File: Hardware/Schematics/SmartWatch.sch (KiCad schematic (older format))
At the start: 104 parts, among them J1 USB_C_Receptacle, J2 PIC32_ICSP, M1 Motor_DC, Q1 Photo_NPN, Q2 2N7000, SW1 SW_Push, SW2 SW_Push, U1 BQ25010, U2 PIC32MZ2048EFG064, U3 STMPE811, U4 nRF8001, U5 LSM303AGR, Y1 80MHz, Y2 32.768kHz, Y3 16MHz

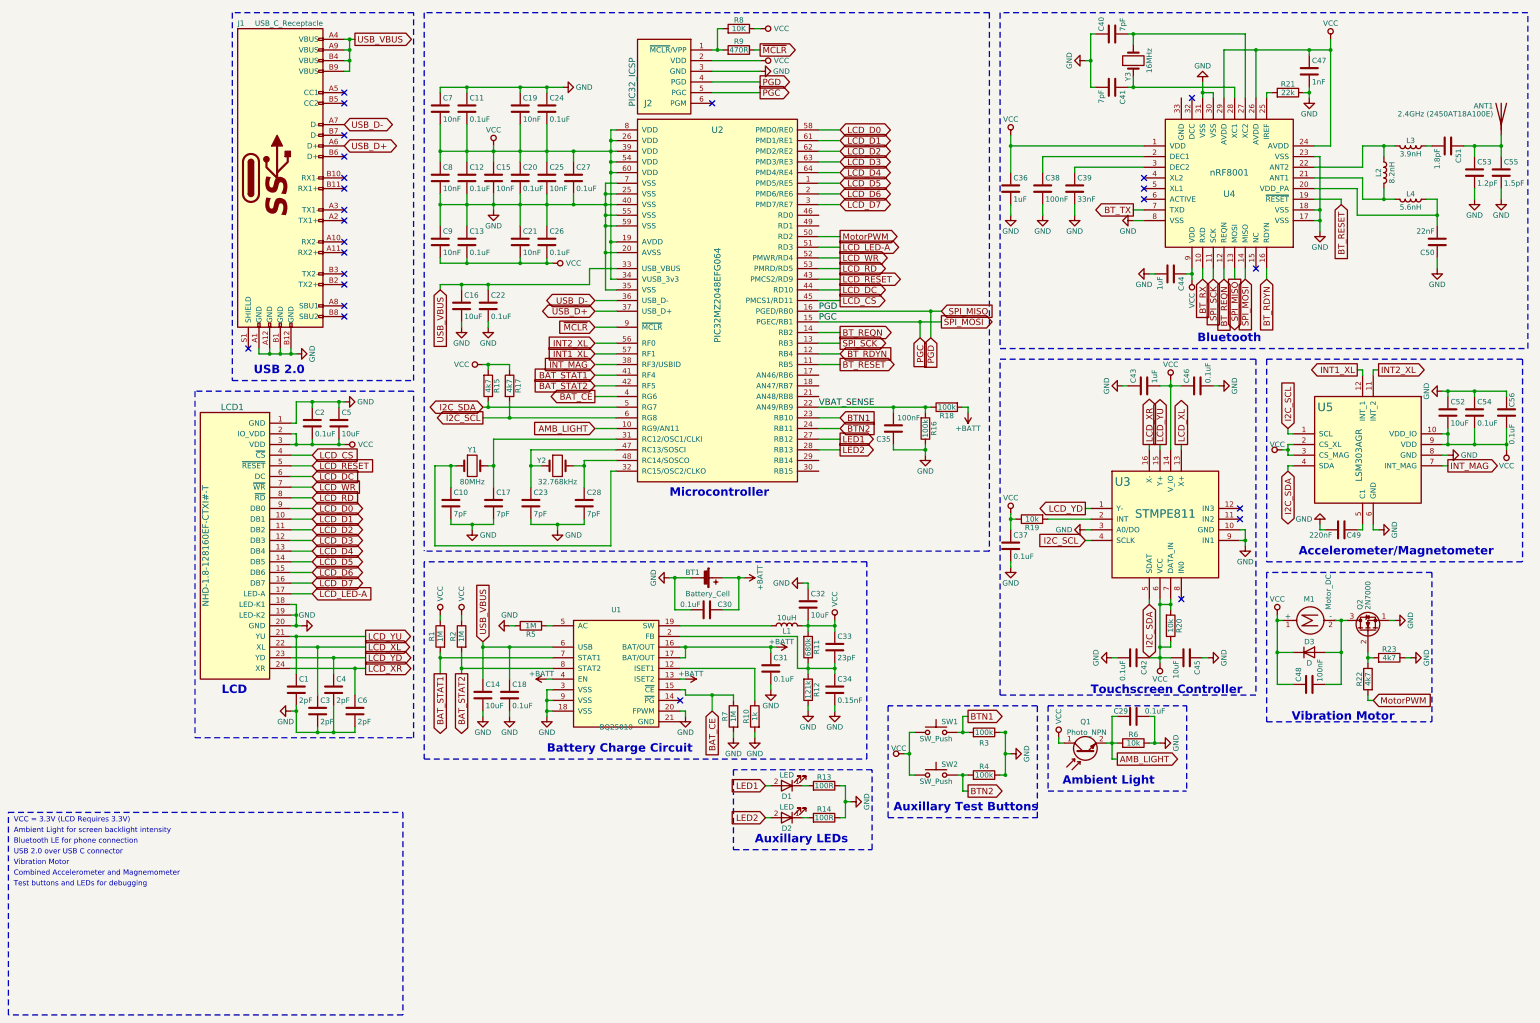
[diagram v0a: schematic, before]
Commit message: fixed file organization
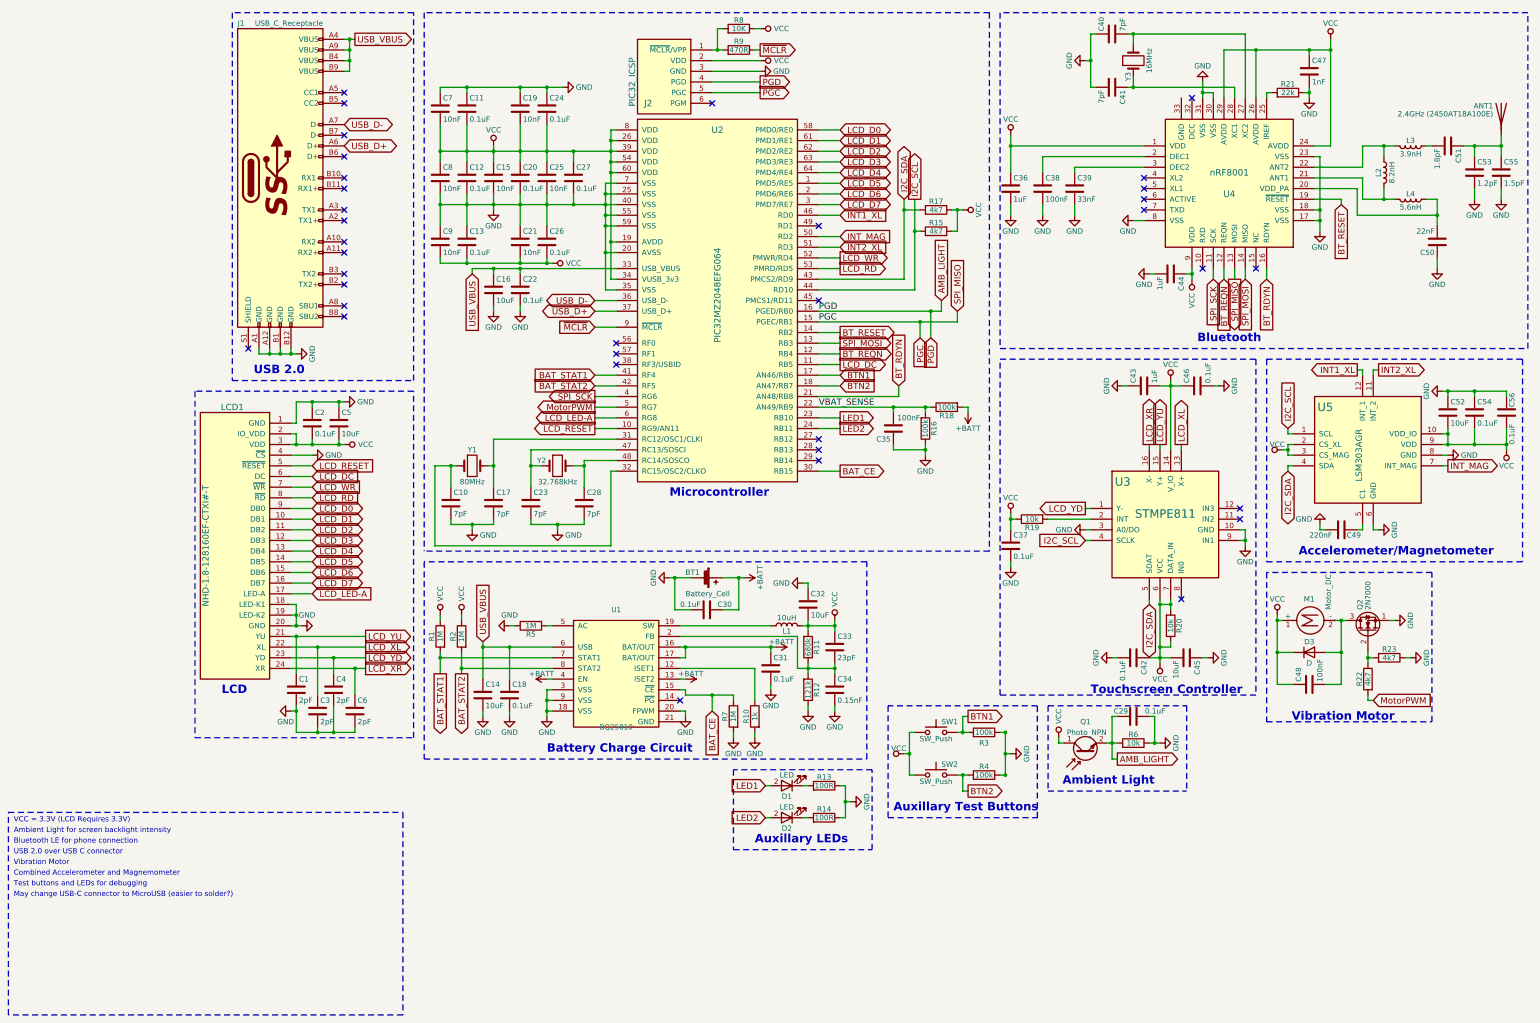
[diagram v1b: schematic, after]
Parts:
- BT1, M1: footprint (none) -> Pin_Headers:Pin_Header_Straight_2x01_Pitch2.54mm_SMD
- C1, C10, C11, C12, C13, C14, C15, C16, C17, C18, C19, C2, C20, C21, C22, C23, C24, C25, C26, C27, C28, C29, C3, C30, C31, C32, C33, C34, C35, C36, C37, C38, C39, C4, C40, C41, C42, C43, C44, C45, C46, C47, C48, C49, C5, C50, C51, C52, C53, C54, C55, C56, C6, C7, C8, C9: footprint (none) -> Capacitors_SMD:C_0805_HandSoldering
- D1, D2: footprint (none) -> LEDs:LED_0805_HandSoldering
- D3: footprint (none) -> Diodes_SMD:D_0805
- J1: footprint (none) -> Connectors_USB:USB_C_Receptacle_Amphenol_12401548E4-2A_CircularHoles
- J2: footprint (none) -> Pin_Headers:Pin_Header_Straight_2x03_Pitch1.00mm_SMD
- L1, L2, L3, L4: footprint (none) -> Inductors_SMD:L_0805_HandSoldering
- Q1: footprint (none) -> Diodes_SMD:D_3220
- R1, R10, R11, R12, R13, R14, R15, R16, R17, R18, R19, R2, R20, R21, R22, R23, R3, R4, R5, R6, R7, R8, R9: footprint (none) -> Resistors_SMD:R_0805_HandSoldering
- SW1, SW2: footprint (none) -> Buttons_Switches_SMD:SW_SPST_FSMSM
- U1: footprint (none) -> Schematics:pvqfn-n20
- U2: footprint (none) -> Housings_QFP:TQFP-64_10x10mm_Pitch0.5mm
- U3: footprint (none) -> Housings_DFN_QFN:QFN-20-1EP_4x4mm_Pitch0.5mm
- U4: footprint (none) -> Housings_DFN_QFN:QFN-32-1EP_5x5mm_Pitch0.5mm
- U5: footprint (none) -> Housings_LGA:LGA-12_2x2mm_Pitch0.5mm
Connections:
- net AMB_LIGHT: now also J2.4 (PGD), U2.16 (PGED/RB0); no longer U2.10 (RG9/AN11)
- net BAT_CE: now also U2.30 (RB15); no longer U2.4 (RG6)
- net BTN1: now also U2.17 (AN46/RB6); no longer U2.23 (RB10)
- net BTN2: now also U2.18 (AN47/RB7); no longer U2.24 (RB11)
- net BT_RDYN: now also U2.21 (AN48/RB8); no longer U2.12 (RB4)
- net BT_REQN: now also U2.12 (RB4); no longer U2.14 (RB2)
- net BT_RESET: now also U2.14 (RB2); no longer U2.11 (RB5)
- net GND: now also LCD1.4 (~CS)
- net I2C_SCL: now also R15.2, U2.44 (RD10); no longer R17.2, U2.6 (RG8)
- net I2C_SDA: now also R17.2, U2.43 (PMCS2/RD9); no longer R15.1, U2.5 (RG7)
- net INT1_XL: now also U2.46 (RD0); no longer U2.57 (RF1)
- net INT2_XL: now also U2.51 (RD3); no longer U2.56 (RF0)
- net INT_MAG: now also U2.50 (RD2); no longer U2.38 (RF3/USBID)
- net LCD_DC: now also U2.11 (RB5); no longer U2.44 (RD10)
- net LCD_LED-A: now also U2.6 (RG8); no longer U2.51 (RD3)
- net LCD_RESET: now also U2.10 (RG9/AN11); no longer U2.43 (PMCS2/RD9)
- net LED1: now also U2.23 (RB10); no longer U2.27 (RB12)
- net LED2: now also U2.24 (RB11); no longer U2.28 (RB13)
- net MotorPWM: now also U2.5 (RG7); no longer U2.50 (RD2)
- net PGC: now also U4.13 (MOSI); no longer U4.14 (MISO)
- net SPI_SCK: now also U2.4 (RG6); no longer U2.13 (RB3)
- net VCC: now also R15.1; no longer R15.2
- net BT_RX: no longer names the net of U4.10 (RXD)
- net BT_TX: no longer names the net of U4.7 (TXD)
- net LCD_CS: no longer names the net of U2.45 (PMCS1/RD11)
- net LCD_CS: no longer LCD1.4 (~CS)
- removed net PGD: J2.4 (PGD), U2.16 (PGED/RB0), U4.13 (MOSI)
- new net SPI_MOSI: U2.13 (RB3), U4.14 (MISO)
- no-connect marks 25 -> 35
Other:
- note added: "May change USB-C connector to MicroUSB (easier to solder?)"
- moved on the sheet: C16, C22, R15, R17

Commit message: finish footprint selecting and started pcb
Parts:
- removed Y3: 16MHz, symbol Crystal
- added Y3: Crystal_GND24, symbol Crystal_GND24
- ANT1: footprint (none) -> 2450AT18A100E:2450AT18A100E
- C10, C17: value 7pF -> 20pF
- C23, C28: value 7pF -> 12.5pF
- C40, C41: value 7pF -> 10pF
- Y1: value 80MHz -> 64MHz; footprint (none) -> Crystals:Crystal_SMD_HC49-SD_HandSoldering
- Y2: footprint (none) -> 2450AT18A100E:TFA322PG327KR
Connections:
- net GND: now also Y3.2, Y3.4
- net at C40.2, U4.27 (XC2): now also Y3.1
- net at C41.1, U4.28 (XC1): now also Y3.3

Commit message: Working on schematic
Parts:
- removed C11, C12, C13, C22, C31: 0.1uF, Capacitors_SMD:C_0805_HandSoldering, symbol C
- removed C16: 10uF, Capacitors_SMD:C_0805_HandSoldering, symbol C
- removed C35: 100nF, Capacitors_SMD:C_0805_HandSoldering, symbol C
- removed C7, C8, C9: 10nF, Capacitors_SMD:C_0805_HandSoldering, symbol C
- removed R20: 10k, Resistors_SMD:R_0805_HandSoldering, symbol R
- C1: renamed from C40; footprint Capacitors_SMD:C_0805_HandSoldering -> Capacitors_SMD:C_0603
- C10: renamed from C20; footprint Capacitors_SMD:C_0805_HandSoldering -> Capacitors_SMD:C_0603
- C11: renamed from C25; footprint Capacitors_SMD:C_0805_HandSoldering -> Capacitors_SMD:C_0603
- C12: renamed from C27; footprint Capacitors_SMD:C_0805_HandSoldering -> Capacitors_SMD:C_0603
- C13: renamed from C36; footprint Capacitors_SMD:C_0805_HandSoldering -> Capacitors_SMD:C_0603
- C14: renamed from C38; footprint Capacitors_SMD:C_0805_HandSoldering -> Capacitors_SMD:C_0603
- C15: renamed from C39; footprint Capacitors_SMD:C_0805_HandSoldering -> Capacitors_SMD:C_0603
- C16: renamed from C21; footprint Capacitors_SMD:C_0805_HandSoldering -> Capacitors_SMD:C_0603
- C17: renamed from C26; footprint Capacitors_SMD:C_0805_HandSoldering -> Capacitors_SMD:C_0603
- C18: renamed from C50; footprint Capacitors_SMD:C_0805_HandSoldering -> Capacitors_SMD:C_0603
- C19: renamed from C44; footprint Capacitors_SMD:C_0805_HandSoldering -> Capacitors_SMD:C_0603
- C2: renamed from C47; footprint Capacitors_SMD:C_0805_HandSoldering -> Capacitors_SMD:C_0603
- C20: renamed from C43; footprint Capacitors_SMD:C_0805_HandSoldering -> Capacitors_SMD:C_0603
- C21: renamed from C46; footprint Capacitors_SMD:C_0805_HandSoldering -> Capacitors_SMD:C_0603
- C22: renamed from C52; footprint Capacitors_SMD:C_0805_HandSoldering -> Capacitors_SMD:C_0603
- C23: renamed from C54; footprint Capacitors_SMD:C_0805_HandSoldering -> Capacitors_SMD:C_0603
- C24: renamed from C56; footprint Capacitors_SMD:C_0805_HandSoldering -> Capacitors_SMD:C_0603
- C25: renamed from C2; footprint Capacitors_SMD:C_0805_HandSoldering -> Capacitors_SMD:C_0603
- C26: renamed from C5; footprint Capacitors_SMD:C_0805_HandSoldering -> Capacitors_SMD:C_0603
- C28: renamed from C10; footprint Capacitors_SMD:C_0805_HandSoldering -> Capacitors_SMD:C_0603
- C29: renamed from C17; footprint Capacitors_SMD:C_0805_HandSoldering -> Capacitors_SMD:C_0603
- C3: renamed from C41; footprint Capacitors_SMD:C_0805_HandSoldering -> Capacitors_SMD:C_0603
- C30: renamed from C23; footprint Capacitors_SMD:C_0805_HandSoldering -> Capacitors_SMD:C_0603
- C31: renamed from C28; footprint Capacitors_SMD:C_0805_HandSoldering -> Capacitors_SMD:C_0603
- C32: renamed from C49; footprint Capacitors_SMD:C_0805_HandSoldering -> Capacitors_SMD:C_0603
- C33: renamed from C37; footprint Capacitors_SMD:C_0805_HandSoldering -> Capacitors_SMD:C_0603
- C34: renamed from C32; footprint Capacitors_SMD:C_0805_HandSoldering -> Capacitors_SMD:C_0603
- C35: renamed from C30; footprint Capacitors_SMD:C_0805_HandSoldering -> Capacitors_SMD:C_0603
- C36: renamed from C33; footprint Capacitors_SMD:C_0805_HandSoldering -> Capacitors_SMD:C_0603
- C37: renamed from C42; footprint Capacitors_SMD:C_0805_HandSoldering -> Capacitors_SMD:C_0603
- C38: renamed from C45; footprint Capacitors_SMD:C_0805_HandSoldering -> Capacitors_SMD:C_0603
- C39: renamed from C48; footprint Capacitors_SMD:C_0805_HandSoldering -> Capacitors_SMD:C_0603
- C4: renamed from C19; footprint Capacitors_SMD:C_0805_HandSoldering -> Capacitors_SMD:C_0603
- C40: renamed from C1; footprint Capacitors_SMD:C_0805_HandSoldering -> Capacitors_SMD:C_0603
- C41: renamed from C4; footprint Capacitors_SMD:C_0805_HandSoldering -> Capacitors_SMD:C_0603
- C42: renamed from C34; footprint Capacitors_SMD:C_0805_HandSoldering -> Capacitors_SMD:C_0603
- C43: renamed from C14; footprint Capacitors_SMD:C_0805_HandSoldering -> Capacitors_SMD:C_0603
- C44: renamed from C18; footprint Capacitors_SMD:C_0805_HandSoldering -> Capacitors_SMD:C_0603
- C45: renamed from C3; footprint Capacitors_SMD:C_0805_HandSoldering -> Capacitors_SMD:C_0603
- C46: renamed from C6; footprint Capacitors_SMD:C_0805_HandSoldering -> Capacitors_SMD:C_0603
- C47: renamed from C29; footprint Capacitors_SMD:C_0805_HandSoldering -> Capacitors_SMD:C_0603
- C5: renamed from C24; footprint Capacitors_SMD:C_0805_HandSoldering -> Capacitors_SMD:C_0603
- C6: renamed from C51; footprint Capacitors_SMD:C_0805_HandSoldering -> Capacitors_SMD:C_0603
- C7: renamed from C53; footprint Capacitors_SMD:C_0805_HandSoldering -> Capacitors_SMD:C_0603
- C8: renamed from C55; footprint Capacitors_SMD:C_0805_HandSoldering -> Capacitors_SMD:C_0603
- C9: renamed from C15; footprint Capacitors_SMD:C_0805_HandSoldering -> Capacitors_SMD:C_0603
- D1: renamed from D3; footprint Diodes_SMD:D_0805 -> Diodes_SMD:D_0603
- D2: renamed from D1; footprint LEDs:LED_0805_HandSoldering -> LEDs:LED_0603
- D3: renamed from D2; footprint LEDs:LED_0805_HandSoldering -> LEDs:LED_0603
- L1: renamed from L3; footprint Inductors_SMD:L_0805_HandSoldering -> Inductors_SMD:L_0603
- L2: footprint Inductors_SMD:L_0805_HandSoldering -> Inductors_SMD:L_0603
- L3: renamed from L4; footprint Inductors_SMD:L_0805_HandSoldering -> Inductors_SMD:L_0603
- L4: renamed from L1; footprint Inductors_SMD:L_0805_HandSoldering -> Inductors_SMD:L_0603
- LCD1: footprint (none) -> 2450AT18A100E:NHD-1.8-128160EF-CTXI#-T
- R1: renamed from R8; footprint Resistors_SMD:R_0805_HandSoldering -> Resistors_SMD:R_0603
- R10: renamed from R1; footprint Resistors_SMD:R_0805_HandSoldering -> Resistors_SMD:R_0603
- R11: renamed from R2; footprint Resistors_SMD:R_0805_HandSoldering -> Resistors_SMD:R_0603
- R12: renamed from R11; footprint Resistors_SMD:R_0805_HandSoldering -> Resistors_SMD:R_0603
- R13: renamed from R23; footprint Resistors_SMD:R_0805_HandSoldering -> Resistors_SMD:R_0603
- R14: renamed from R22; footprint Resistors_SMD:R_0805_HandSoldering -> Resistors_SMD:R_0603
- R15: renamed from R12; footprint Resistors_SMD:R_0805_HandSoldering -> Resistors_SMD:R_0603
- R16: renamed from R7; footprint Resistors_SMD:R_0805_HandSoldering -> Resistors_SMD:R_0603
- R17: renamed from R10; footprint Resistors_SMD:R_0805_HandSoldering -> Resistors_SMD:R_0603
- R18: renamed from R3; footprint Resistors_SMD:R_0805_HandSoldering -> Resistors_SMD:R_0603
- R19: renamed from R6; footprint Resistors_SMD:R_0805_HandSoldering -> Resistors_SMD:R_0603
- R2: renamed from R9; footprint Resistors_SMD:R_0805_HandSoldering -> Resistors_SMD:R_0603
- R20: renamed from R4; footprint Resistors_SMD:R_0805_HandSoldering -> Resistors_SMD:R_0603
- R21: renamed from R13; footprint Resistors_SMD:R_0805_HandSoldering -> Resistors_SMD:R_0603
- R22: renamed from R14; footprint Resistors_SMD:R_0805_HandSoldering -> Resistors_SMD:R_0603
- R3: renamed from R21; footprint Resistors_SMD:R_0805_HandSoldering -> Resistors_SMD:R_0603
- R4: renamed from R17; footprint Resistors_SMD:R_0805_HandSoldering -> Resistors_SMD:R_0603
- R5: renamed from R15; footprint Resistors_SMD:R_0805_HandSoldering -> Resistors_SMD:R_0603
- R6: renamed from R18; footprint Resistors_SMD:R_0805_HandSoldering -> Resistors_SMD:R_0603
- R7: renamed from R16; footprint Resistors_SMD:R_0805_HandSoldering -> Resistors_SMD:R_0603
- R8: renamed from R19; footprint Resistors_SMD:R_0805_HandSoldering -> Resistors_SMD:R_0603
- R9: renamed from R5; footprint Resistors_SMD:R_0805_HandSoldering -> Resistors_SMD:R_0603
- Y1: renamed from Y3; footprint (none) -> 2450AT18A100E:CX2520DB16000F0FDFC1
- Y2: renamed from Y1; footprint Crystals:Crystal_SMD_HC49-SD_HandSoldering -> 2450AT18A100E:CX2520DB16000F0FDFC1
- renumbered J2 to J1, J1 to J2, Q2 to Q1, Q1 to Q2, U4 to U1, U5 to U3, U3 to U4, U1 to U5, Y2 to Y3

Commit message: PCB
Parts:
- removed Y2: 64MHz, 2450AT18A100E:CX2520DB16000F0FDFC1, symbol Crystal
- added Y?: Crystal_GND24, 2450AT18A100E:CX2520DB16000F0FDFC1, symbol Crystal_GND24
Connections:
- net GND: now also Y?.2, Y?.4
- net at C29.1, U2.31 (RC12/OSC1/CLKI): now also Y?.1
- net at C28.1, U2.32 (RC15/OSC2/CLKO): now also Y?.3
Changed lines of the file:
@@
 $EndComp
 $Comp
-L Crystal Y2
-U 1 1 5A2813FF
-P 4900 6000
-F 0 "Y2" H 4900 6150 50  0000 C CNN
-F 1 "64MHz" H 4900 5850 50  0000 C CNN
-F 2 "2450AT18A100E:CX2520DB16000F0FDFC1" H 4900 6000 50  0001 C CNN
-F 3 "" H 4900 6000 50  0001 C CNN
-	1    4900 6000
-	1    0    0    -1
-$EndComp
-$Comp
 L C C28
 U 1 1 5A281E18
@@
 	4700 6550 4700 6500
 Wire Wire Line
-	4900 6550 4900 6600
+	4900 6200 4900 6600
 Wire Wire Line
 	4700 6550 5100 6550
@@
 	12050 2450 12050 2550
 Wire Wire Line
-	11050 2450 12050 2450
-Connection ~ 11100 2450
-Wire Wire Line
-	11100 2350 11100 2450
-Wire Wire Line
-	11100 2050 11100 1950
-Wire Wire Line
-	11050 1950 12150 1950
-Wire Wire Line
 	12150 1950 12150 2550
-Connection ~ 11100 1950
 Wire Wire Line
 	10700 1950 10700 2450
@@
 Wire Wire Line
 	11450 7300 11450 7250
+Wire Wire Line
+	12050 2450 11050 2450
+Wire Wire Line
+	11050 1950 12150 1950
+Wire Wire Line
+	11100 2050 11100 1950
+Connection ~ 11100 1950
+Wire Wire Line
+	11100 2350 11100 2450
+Connection ~ 11100 2450
+$Comp
+L Crystal_GND24 Y?
+U 1 1 5A615765
+P 4900 6000
+F 0 "Y?" H 5025 6200 50  0000 L CNN
+F 1 "Crystal_GND24" H 4750 5700 50  0000 L CNN
+F 2 "2450AT18A100E:CX2520DB16000F0FDFC1" H 4900 6000 50  0001 C CNN
+F 3 "" H 4900 6000 50  0001 C CNN
+	1    4900 6000
+	-1   0    0    1
+$EndComp
+$Comp
+L GND #PWR?
+U 1 1 5A6162C7
+P 4900 5750
+F 0 "#PWR?" H 4900 5500 50  0001 C CNN
+F 1 "GND" H 5050 5700 50  0000 C CNN
+F 2 "" H 4900 5750 50  0001 C CNN
+F 3 "" H 4900 5750 50  0001 C CNN
+	1    4900 5750
+	-1   0    0    1
+$EndComp
+Wire Wire Line
+	4900 5800 4900 5750
 $EndSCHEMATC

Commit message: cant remember
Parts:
- removed C33: 0.1uF, Capacitors_SMD:C_0603, symbol C
- removed R8: 10k, Resistors_SMD:R_0603, symbol R
- gave numbers to parts that had none: 1
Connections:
- net GND: now also U1.33 (GND), U5.21 (GND)
- net T_INT: now reaches U2.56 (RF0)
- net T_INT: now also U4.2 (INT)
- no-connect marks 35 -> 34
